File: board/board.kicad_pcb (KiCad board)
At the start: 2 copper layers, 10 parts, among them SW1 Push_Button, SW2 Push_Button, SW3 Push_Button, U1 ATtiny85-20P

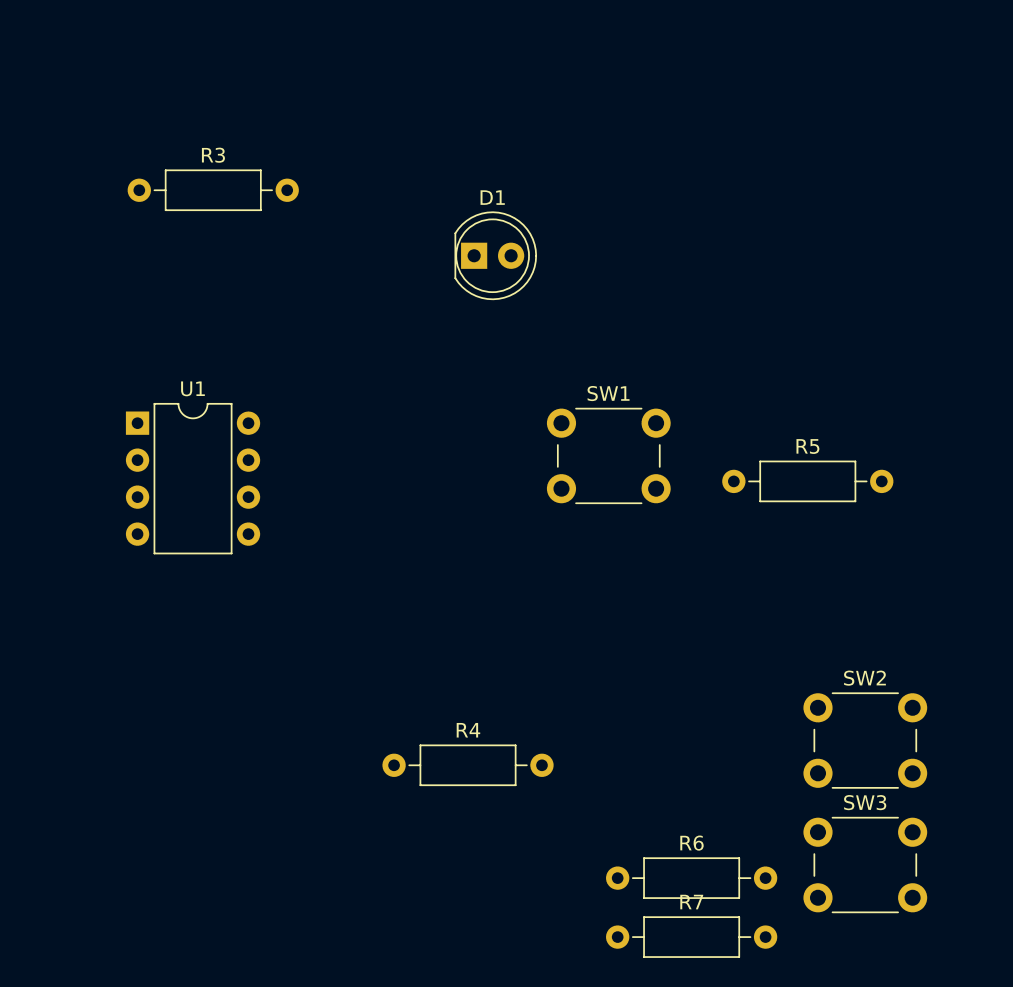
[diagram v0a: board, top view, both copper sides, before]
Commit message: Creating PCB for 'THE BUTTON'
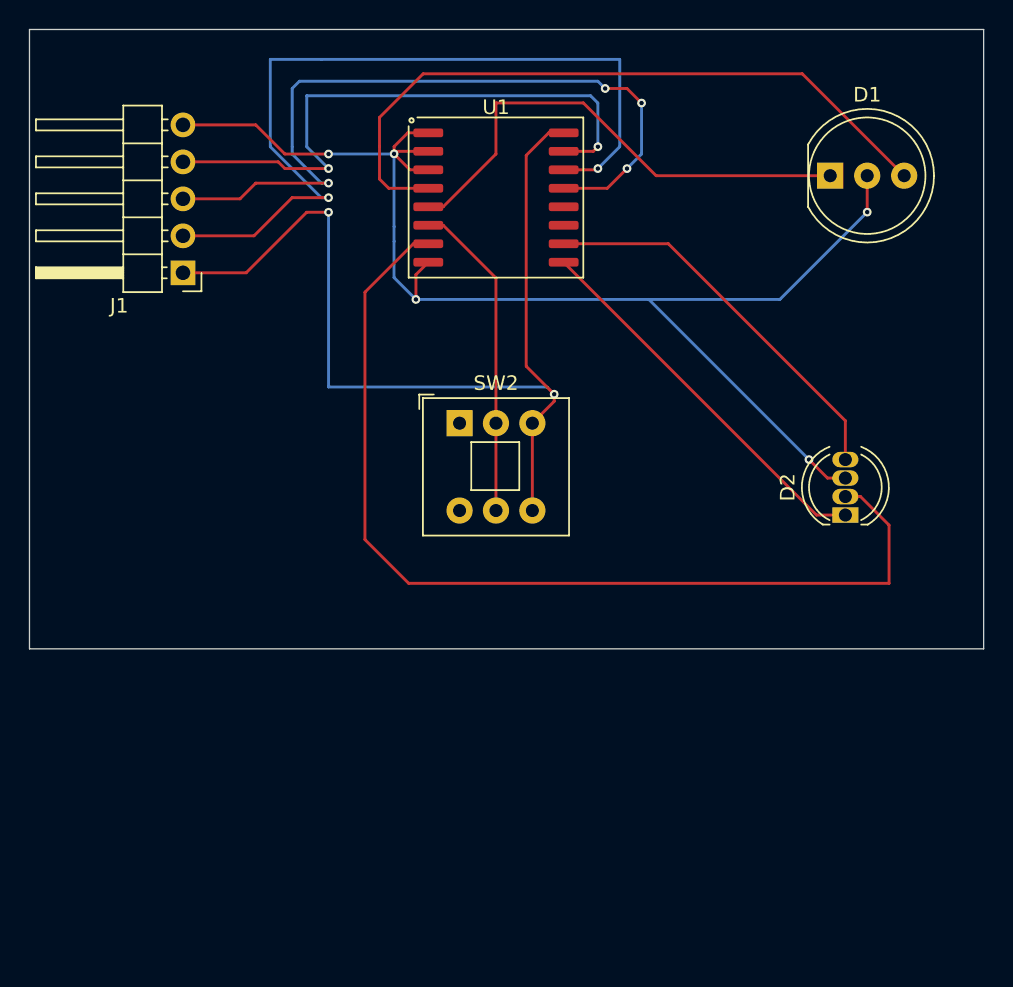
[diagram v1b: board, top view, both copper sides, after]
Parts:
- removed R3: 1.8k, Resistor_THT:R_Axial_DIN0207_L6.3mm_D2.5mm_P10.16mm_Horizontal
- removed R4: 1k, Resistor_THT:R_Axial_DIN0207_L6.3mm_D2.5mm_P10.16mm_Horizontal
- removed R5, R6, R7: 470ohm, Resistor_THT:R_Axial_DIN0207_L6.3mm_D2.5mm_P10.16mm_Horizontal
- removed SW1, SW3: Push_Button, Button_Switch_THT:SW_PUSH_6mm
- added D2: LED_GBKR, LED_THT:LED_D5.0mm-4_RGB, F.Cu at (79.5, 49.3)
- added J1: PINHD_1x5_Male, Connector_PinHeader_2.54mm:PinHeader_1x05_P2.54mm_Horizontal, F.Cu at (34.0, 32.7)
- D1: value LED -> LED_Dual_AKA; footprint LED_THT:LED_D5.0mm -> LED_THT:LED_D8.0mm-3
- SW2: value Push_Button -> SW_Push_DPDT; footprint Button_Switch_THT:SW_PUSH_6mm -> Button_Switch_THT:SW_Push_2P2T_Toggle_CK_PVA2xxH1xxxxxxV2
- U1: value ATtiny85-20P -> PCF8574; footprint Package_DIP:DIP-8_W7.62mm -> PCM_Package_SO_AKL:SOIC-16W_7.5x10.3mm_P1.27mm
- moved SW2 31.4 mm to (53.0, 43.0)
- moved U1 29.1 mm to (55.5, 27.5)
- moved D1 25.1 mm to (78.5, 26.0)
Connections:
- D1 pad 1: Net-(D1-Pad1) -> Net-(D1-A1)
- D1 pad 2: Net-(U1-PB1) -> /The Button/GND
- SW2 pad 1: Net-(U1-PB2) -> unconnected-(SW2-A-Pad1)
- SW2 pad 2: Net-(R6-Pad2) -> Net-(U1-P2)
- U1 pad 1: unconnected-(U1-~{RESET}/PB5-Pad1) -> /The Button/GND
- U1 pad 2: /SCL -> /The Button/GND
- U1 pad 3: unconnected-(U1-XTAL2/PB4-Pad3) -> /The Button/GND
- U1 pad 4: /GND -> Net-(D1-A2)
- U1 pad 5: /SDA -> Net-(D1-A1)
- U1 pad 6: Net-(U1-PB1) -> Net-(U1-P2)
- U1 pad 7: Net-(U1-PB2) -> Net-(D2-BA)
- U1 pad 8: /VCC -> /The Button/GND
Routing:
- net /The Button/GND: track 0.00 -> 92.0 mm, vias 0 -> 5
- net /The Button/VCC: track 0.00 -> 68.5 mm, vias 0 -> 2
- net Net-(D2-BA): track 0.00 -> 67.8 mm
- net /The Button/SCL: track 0.00 -> 57.0 mm, vias 0 -> 2
- net /The Button/~{INT}: track 0.00 -> 52.9 mm, vias 0 -> 4
- net Net-(D1-A2): track 0.00 -> 48.0 mm
- net /The Button/SDA: track 0.00 -> 41.5 mm, vias 0 -> 2
- net Net-(D1-A1): track 0.00 -> 34.7 mm
- net Net-(D2-RA): track 0.00 -> 27.1 mm
- net Net-(D2-GA): track 0.00 -> 26.5 mm
- net Net-(U1-P2): track 0.00 -> 22.1 mm
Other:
- board outline added: 65.5 x 42.5 mm
